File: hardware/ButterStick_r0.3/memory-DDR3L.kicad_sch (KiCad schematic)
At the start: 0 parts

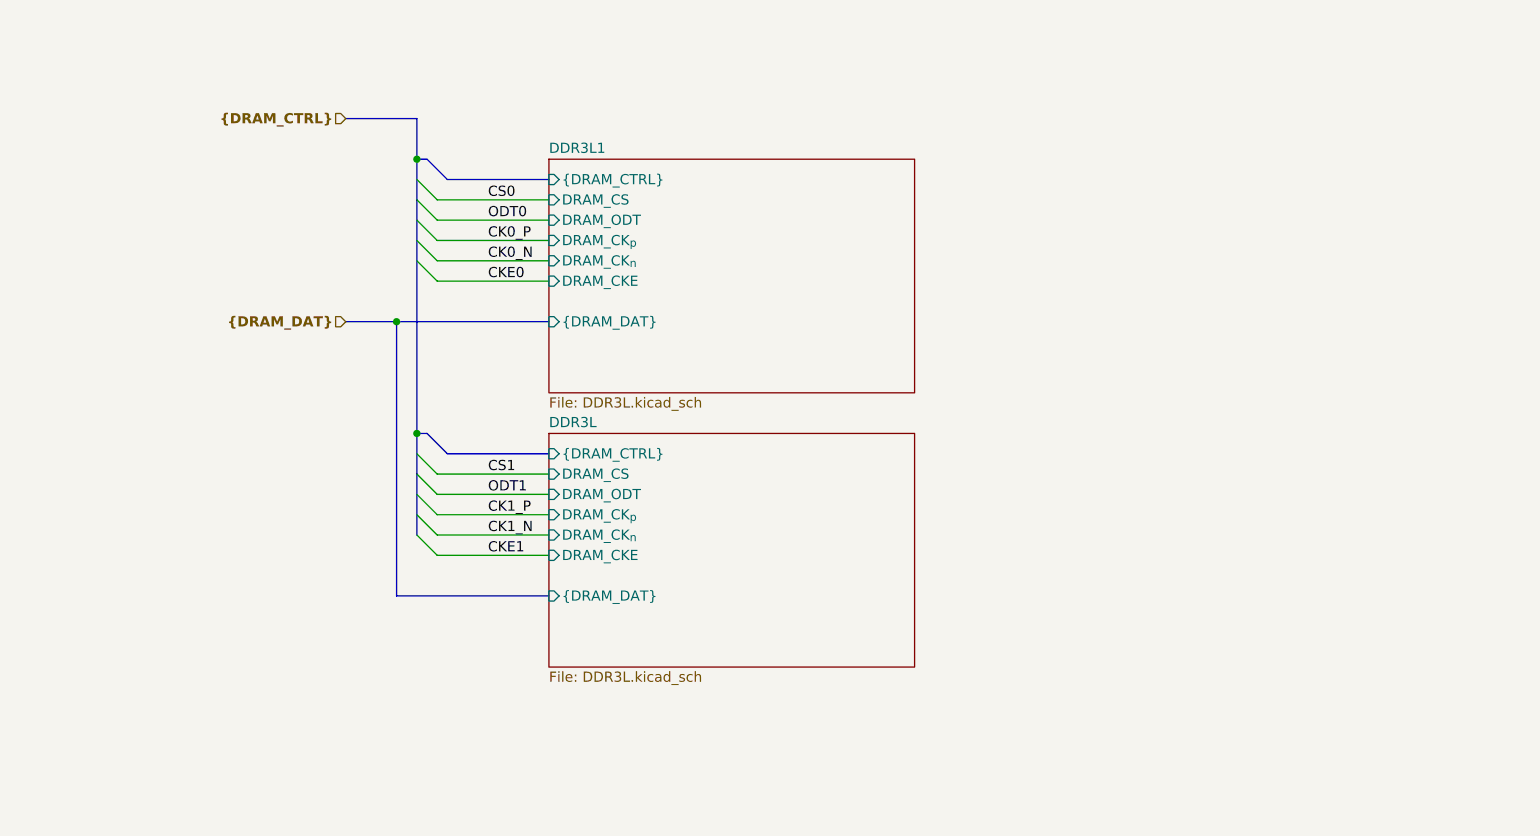
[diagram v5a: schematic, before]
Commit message: hw.r0d3: Length matched all SYZYGY ports
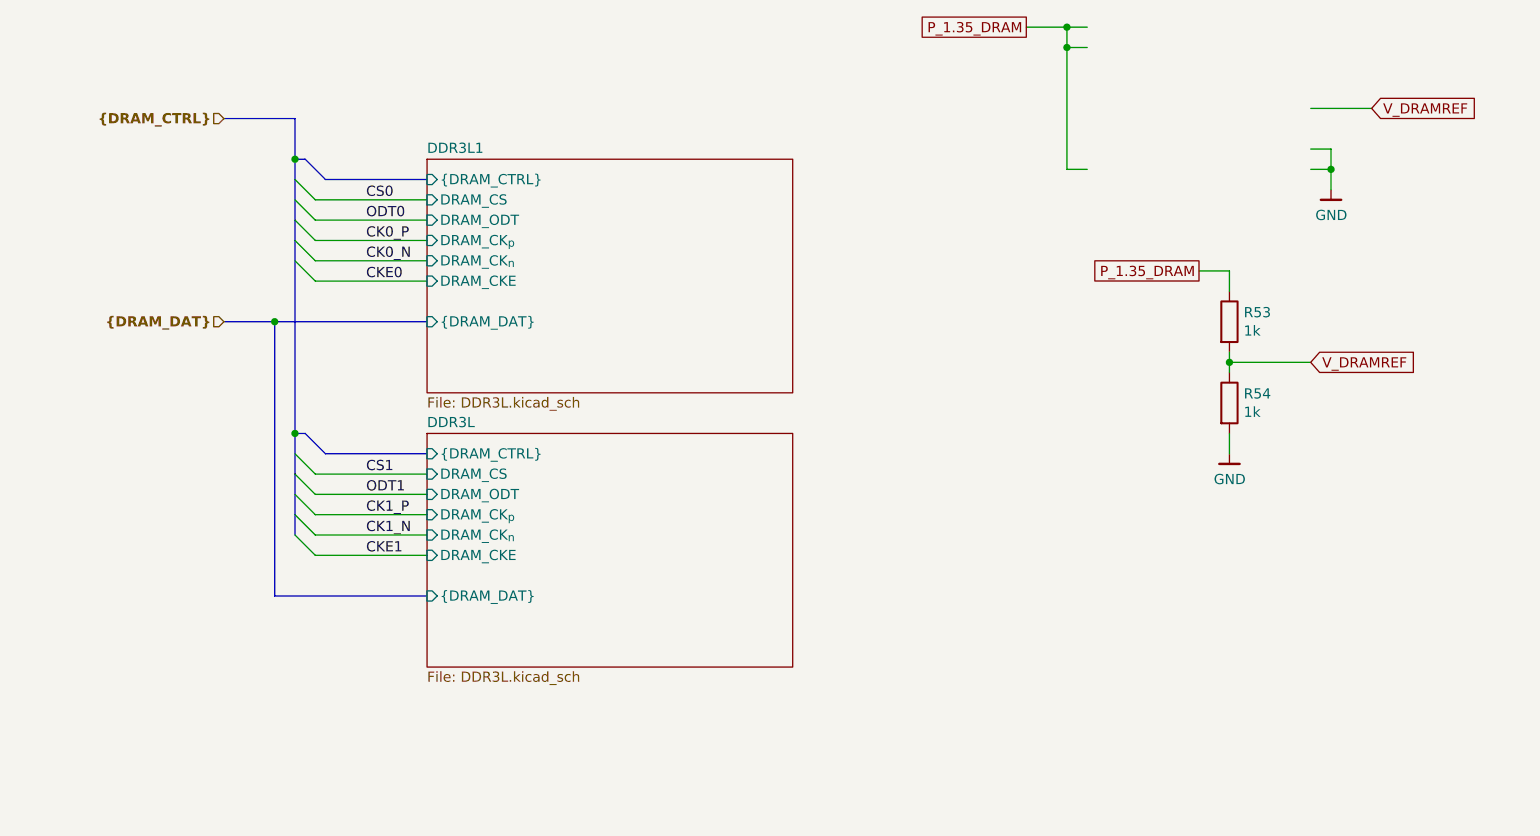
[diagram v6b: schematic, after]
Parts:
- added R53, R54: 1k, Resistor_SMD:R_0402_1005Metric, symbol Device:R
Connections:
- new net GND: R54.2
- new net P_1.35_DRAM: R53.1
- new net V_DRAMREF: R53.2, R54.1

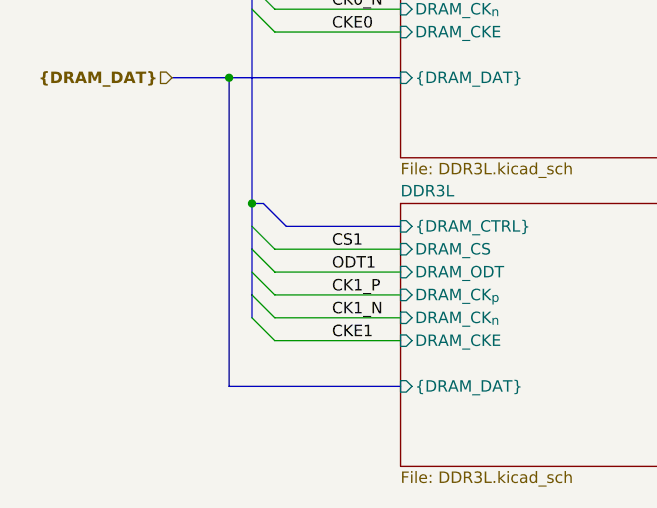
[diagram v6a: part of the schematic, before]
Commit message: hw.r0d3: update routing
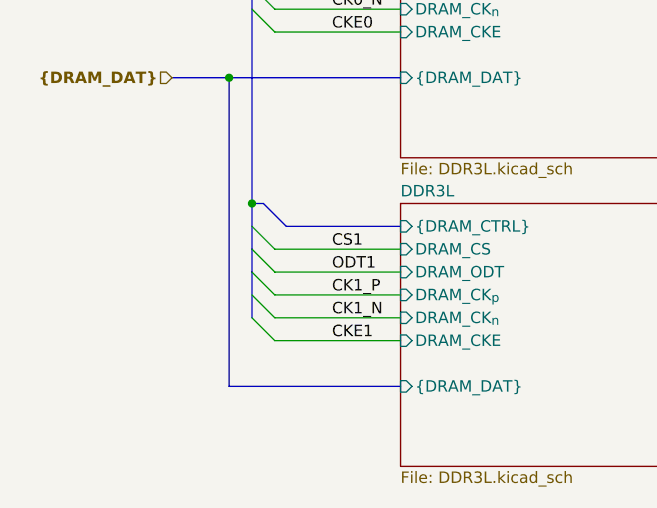
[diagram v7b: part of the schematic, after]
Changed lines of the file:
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@@
 (kicad_sch (version 20200608) (host eeschema "5.99.0-unknown-08c61e6~101~ubuntu18.04.1")
-  (page 12 19)
+  (page 1 19)
   (paper "A4")
   (title_block
@@
     (stroke (width 0) (type solid) (color 0 0 0 0))
   )
-  (bus (pts (xy 80.01 104.14) (xy 80.01 109.22))
+  (bus (pts (xy 80.01 104.14) (xy 80.01 106.68))
     (stroke (width 0) (type solid) (color 0 0 0 0))
   )
-  (bus (pts (xy 80.01 109.22) (xy 80.01 111.76))
+  (bus (pts (xy 80.01 106.68) (xy 80.01 111.76))
     (stroke (width 0) (type solid) (color 0 0 0 0))
   )

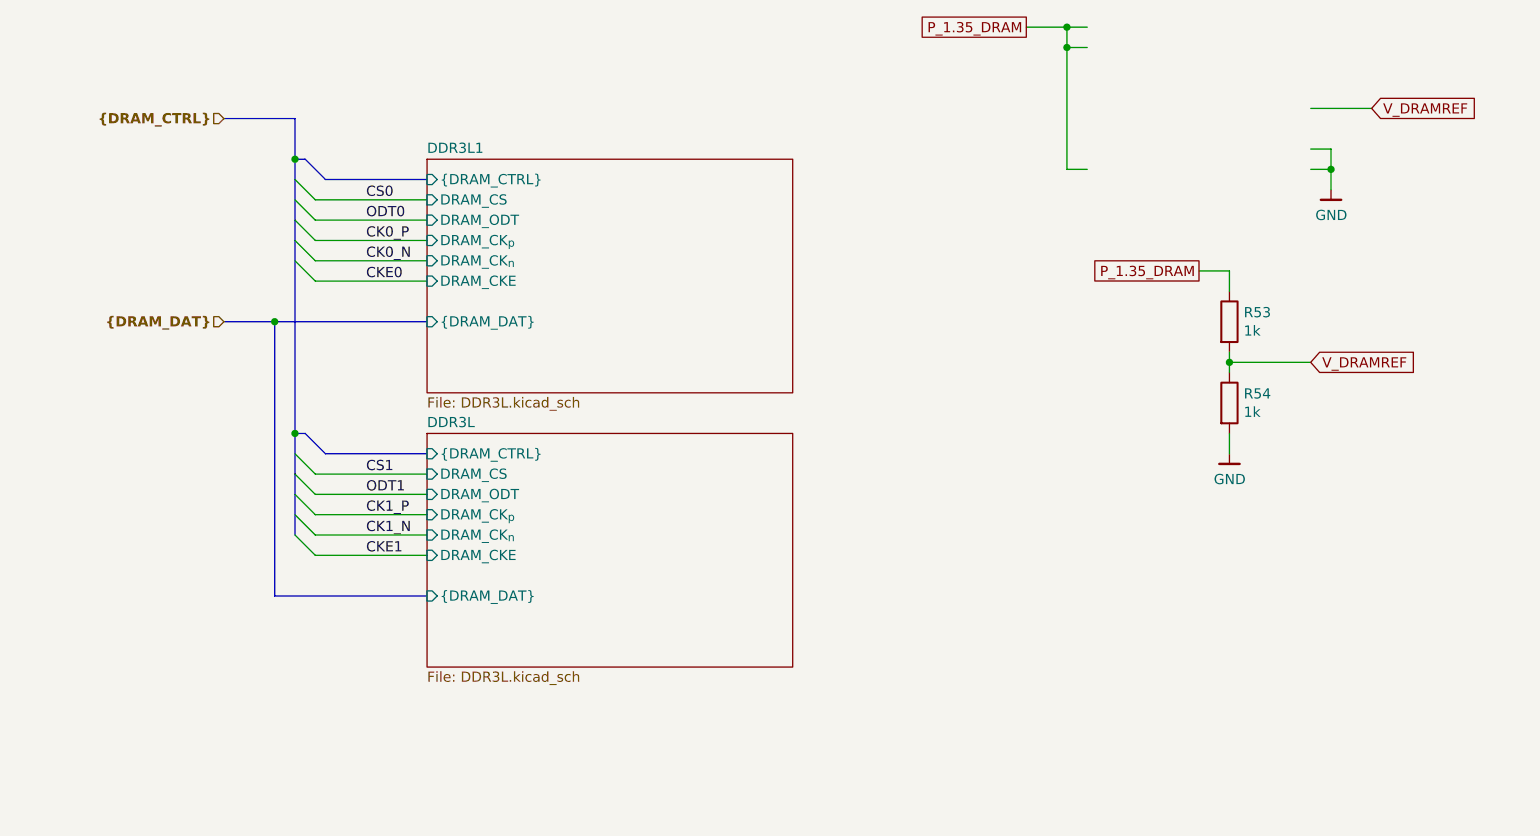
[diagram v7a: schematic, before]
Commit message: hw.r0d3: Continue routing
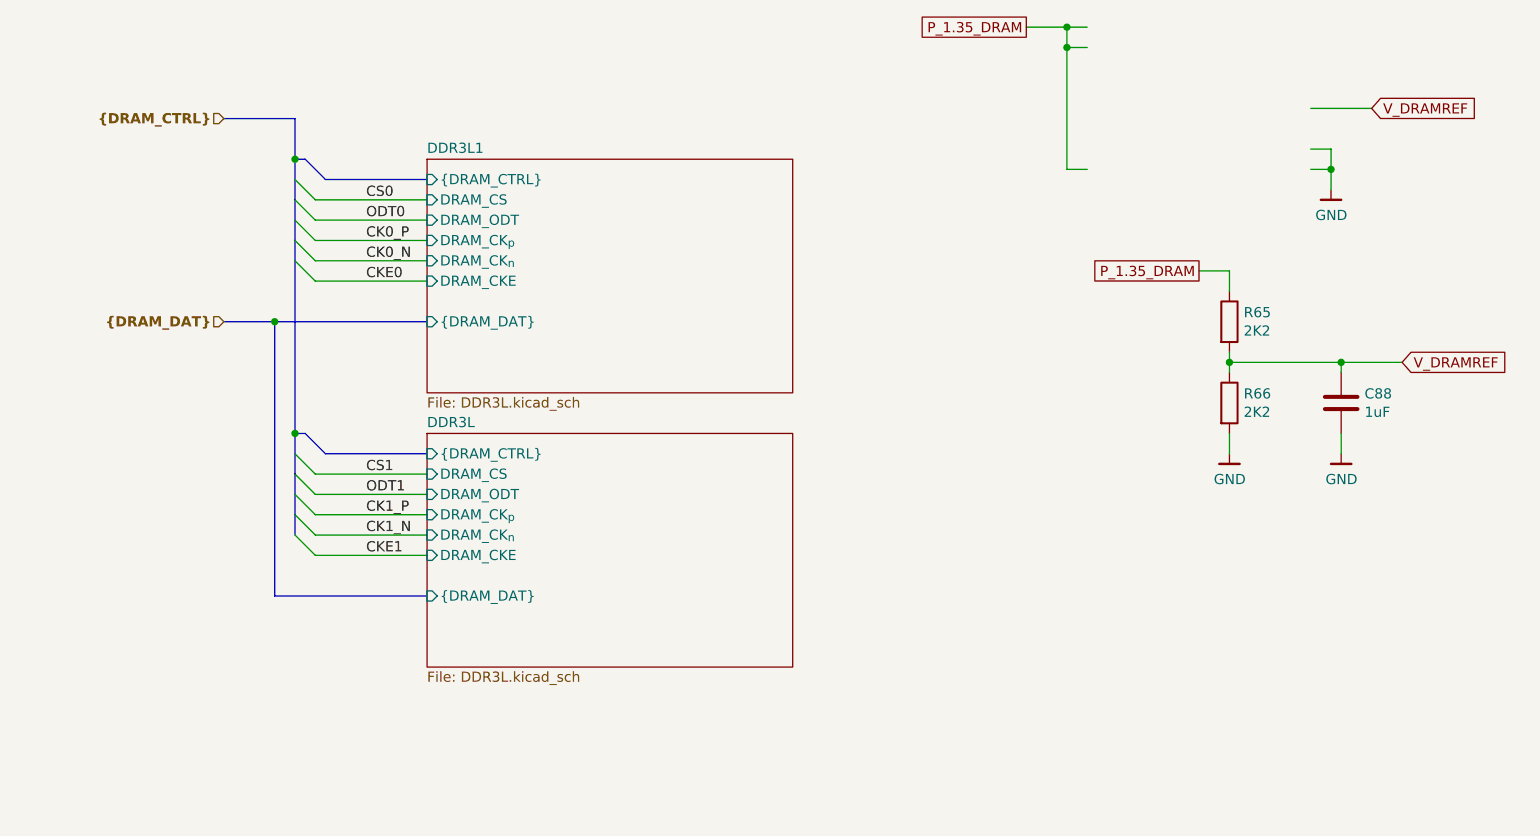
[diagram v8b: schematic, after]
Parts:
- added C88: 1uF, Capacitor_SMD:C_0402_1005Metric, symbol Device:C
- R65: renamed from R53; value 1k -> 2K2
- R66: renamed from R54; value 1k -> 2K2
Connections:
- net GND: now also C88.2
- net V_DRAMREF: now also C88.1
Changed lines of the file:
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@@
 (kicad_sch (version 20200608) (host eeschema "5.99.0-unknown-08c61e6~101~ubuntu18.04.1")
-  (page 1 19)
+  (page 13 19)
   (paper "A4")
   (title_block
@@
   (junction (at 196.85 90.17))
   (junction (at 209.55 66.04))
+  (junction (at 210.82 90.17))
   (junction (at 77.47 85.09))
   (junction (at 80.01 64.77))
@@
     (stroke (width 0) (type solid) (color 0 0 0 0))
   )
-  (wire (pts (xy 196.85 90.17) (xy 207.01 90.17))
+  (wire (pts (xy 196.85 90.17) (xy 210.82 90.17))
     (stroke (width 0) (type solid) (color 0 0 0 0))
   )
@@
     (stroke (width 0) (type solid) (color 0 0 0 0))
   )
+  (wire (pts (xy 210.82 90.17) (xy 210.82 91.44))
+    (stroke (width 0) (type solid) (color 0 0 0 0))
+  )
+  (wire (pts (xy 210.82 90.17) (xy 218.44 90.17))
+    (stroke (width 0) (type solid) (color 0 0 0 0))
+  )
+  (wire (pts (xy 210.82 99.06) (xy 210.82 101.6))
+    (stroke (width 0) (type solid) (color 0 0 0 0))
+  )
   (bus (pts (xy 71.12 59.69) (xy 80.01 59.69))
     (stroke (width 0) (type solid) (color 0 0 0 0))
@@
     (stroke (width 0) (type solid) (color 0 0 0 0))
   )
-  (bus (pts (xy 80.01 64.77) (xy 80.01 67.31))
+  (bus (pts (xy 80.01 64.77) (xy 80.01 69.85))
     (stroke (width 0) (type solid) (color 0 0 0 0))
   )
@@
     (stroke (width 0) (type solid) (color 0 0 0 0))
   )
-  (bus (pts (xy 80.01 67.31) (xy 80.01 72.39))
-    (stroke (width 0) (type solid) (color 0 0 0 0))
-  )
-  (bus (pts (xy 80.01 72.39) (xy 80.01 74.93))
+  (bus (pts (xy 80.01 69.85) (xy 80.01 74.93))
     (stroke (width 0) (type solid) (color 0 0 0 0))
   )
@@
     (stroke (width 0) (type solid) (color 0 0 0 0))
   )
-  (bus (pts (xy 80.01 104.14) (xy 80.01 106.68))
-    (stroke (width 0) (type solid) (color 0 0 0 0))
-  )
-  (bus (pts (xy 80.01 106.68) (xy 80.01 111.76))
+  (bus (pts (xy 80.01 104.14) (xy 80.01 109.22))
+    (stroke (width 0) (type solid) (color 0 0 0 0))
+  )
+  (bus (pts (xy 80.01 109.22) (xy 80.01 111.76))
     (stroke (width 0) (type solid) (color 0 0 0 0))
   )
@@
     (effects (font (size 1.27 1.27)) (justify right))
   )
-  (global_label "V_DRAMREF" (shape input) (at 207.01 90.17 0)
-    (effects (font (size 1.27 1.27)) (justify left))
-  )
   (global_label "V_DRAMREF" (shape input) (at 214.63 58.42 0)
     (effects (font (size 1.27 1.27)) (justify left))
   )
+  (global_label "V_DRAMREF" (shape input) (at 218.44 90.17 0)
+    (effects (font (size 1.27 1.27)) (justify left))
+  )
   (hierarchical_label "{DRAM_CTRL}" (shape input) (at 71.12 59.69 180)
     (effects (font (size 1.27 1.27) (thickness 0.254) bold) (justify right))
@@
   (symbol (lib_id "gkl_power:GND") (at 196.85 101.6 0) (unit 1)
     (in_bom yes) (on_board yes)
-    (property "Reference" "#PWR094" (id 0) (at 196.85 107.95 0)
+    (property "Reference" "#PWR0148" (id 0) (at 196.85 107.95 0)
       (effects (font (size 1.27 1.27)) hide)
     )
@@
   (symbol (lib_id "gkl_power:GND") (at 209.55 68.58 0) (unit 1)
     (in_bom yes) (on_board yes)
-    (property "Reference" "#PWR095" (id 0) (at 209.55 74.93 0)
+    (property "Reference" "#PWR0149" (id 0) (at 209.55 74.93 0)
       (effects (font (size 1.27 1.27)) hide)
     )
@@
     )
   )
+  (symbol (lib_id "gkl_power:GND") (at 210.82 101.6 0) (unit 1)
+    (in_bom yes) (on_board yes)
+    (property "Reference" "#PWR0150" (id 0) (at 210.82 107.95 0)
+      (effects (font (size 1.27 1.27)) hide)
+    )
+    (property "Value" "GND" (id 1) (at 210.8581 104.8068 0))
+    (property "Footprint" "" (id 2) (at 208.28 110.49 0)
+      (effects (font (size 1.27 1.27)) hide)
+    )
+    (property "Datasheet" "" (id 3) (at 210.82 101.6 0)
+      (effects (font (size 1.27 1.27)) hide)
+    )
+  )
   (symbol (lib_id "Device:R") (at 196.85 85.09 0) (unit 1)
     (in_bom yes) (on_board yes)
-    (property "Reference" "R53" (id 0) (at 198.6281 83.9406 0)
-      (effects (font (size 1.27 1.27)) (justify left))
-    )
-    (property "Value" "1k" (id 1) (at 198.6281 86.2393 0)
+    (property "Reference" "R65" (id 0) (at 198.6281 83.9406 0)
+      (effects (font (size 1.27 1.27)) (justify left))
+    )
+    (property "Value" "2K2" (id 1) (at 198.6281 86.2393 0)
       (effects (font (size 1.27 1.27)) (justify left))
     )
@@
   (symbol (lib_id "Device:R") (at 196.85 95.25 0) (unit 1)
     (in_bom yes) (on_board yes)
-    (property "Reference" "R54" (id 0) (at 198.6281 94.1006 0)
-      (effects (font (size 1.27 1.27)) (justify left))
-    )
-    (property "Value" "1k" (id 1) (at 198.6281 96.3993 0)
+    (property "Reference" "R66" (id 0) (at 198.6281 94.1006 0)
+      (effects (font (size 1.27 1.27)) (justify left))
+    )
+    (property "Value" "2K2" (id 1) (at 198.6281 96.3993 0)
       (effects (font (size 1.27 1.27)) (justify left))
     )
@@
       (effects (font (size 1.27 1.27)) hide)
     )
+  )
+  (symbol (lib_id "Device:C") (at 210.82 95.25 0) (unit 1)
+    (in_bom yes) (on_board yes)
+    (property "Reference" "C88" (id 0) (at 213.7411 94.1006 0)
+      (effects (font (size 1.27 1.27)) (justify left))
+    )
+    (property "Value" "1uF" (id 1) (at 213.7411 96.3993 0)
+      (effects (font (size 1.27 1.27)) (justify left))
+    )
+    (property "Footprint" "Capacitor_SMD:C_0402_1005Metric" (id 2) (at 211.7852 99.06 0)
+      (effects (font (size 1.27 1.27)) hide)
+    )
+    (property "Datasheet" "~" (id 3) (at 210.82 95.25 0)
+      (effects (font (size 1.27 1.27)) hide)
+    )
